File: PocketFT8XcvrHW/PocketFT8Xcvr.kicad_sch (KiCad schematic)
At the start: 55 parts, among them J1 HX8357D SPI, J2 22-23-2021, J3 B5B-XH-A_LF__SN_, J5 HX8357D 8-BIT, Q1 2N7002DW, U1 MCP3422A1T-E/SN, U2 Si4735-D60-GU, U3 SN74ACT244DWR, U4 SI5351C-B-GM, Y1 ASTX-H11-25.000MHZ-T

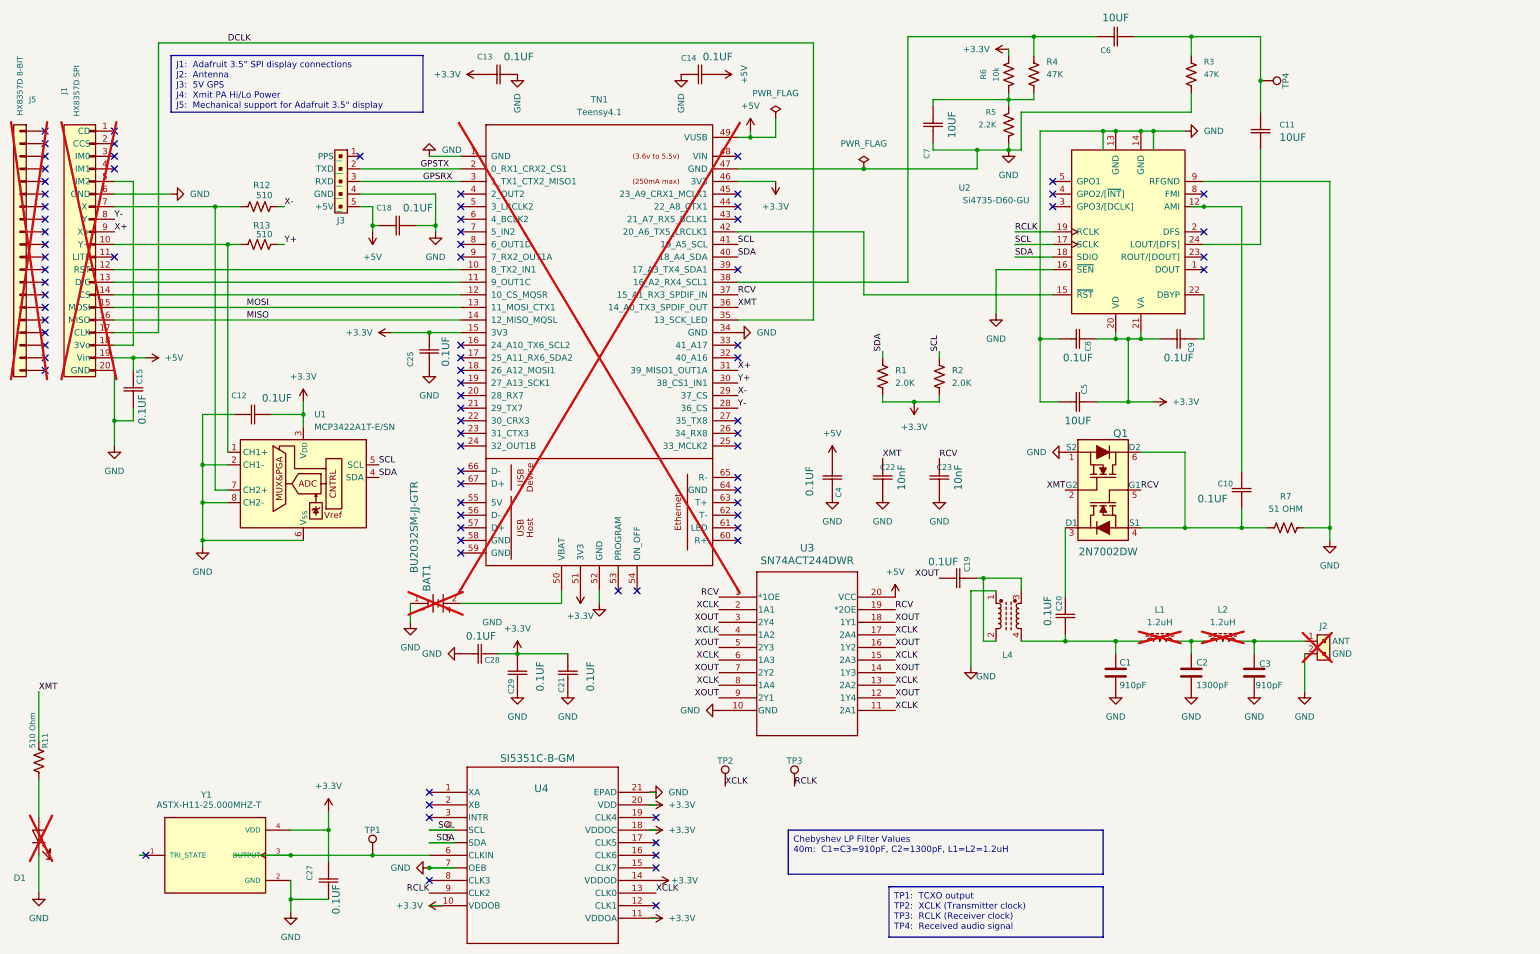
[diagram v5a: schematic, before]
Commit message: Isolate SI4735 I2C traffic from other I2C chips for Issue #23
+ The ADC and SI5351 now reside on SCL2/SDA2.  The SI4735 remains on SCL/SDA.  There are now two I2C bus's.
+ The SI5351 XCLK now drives a single gate re. recommendation for SI5351 phase noise performance.
+ Improved +5V bulk (low frequency) decoupling.
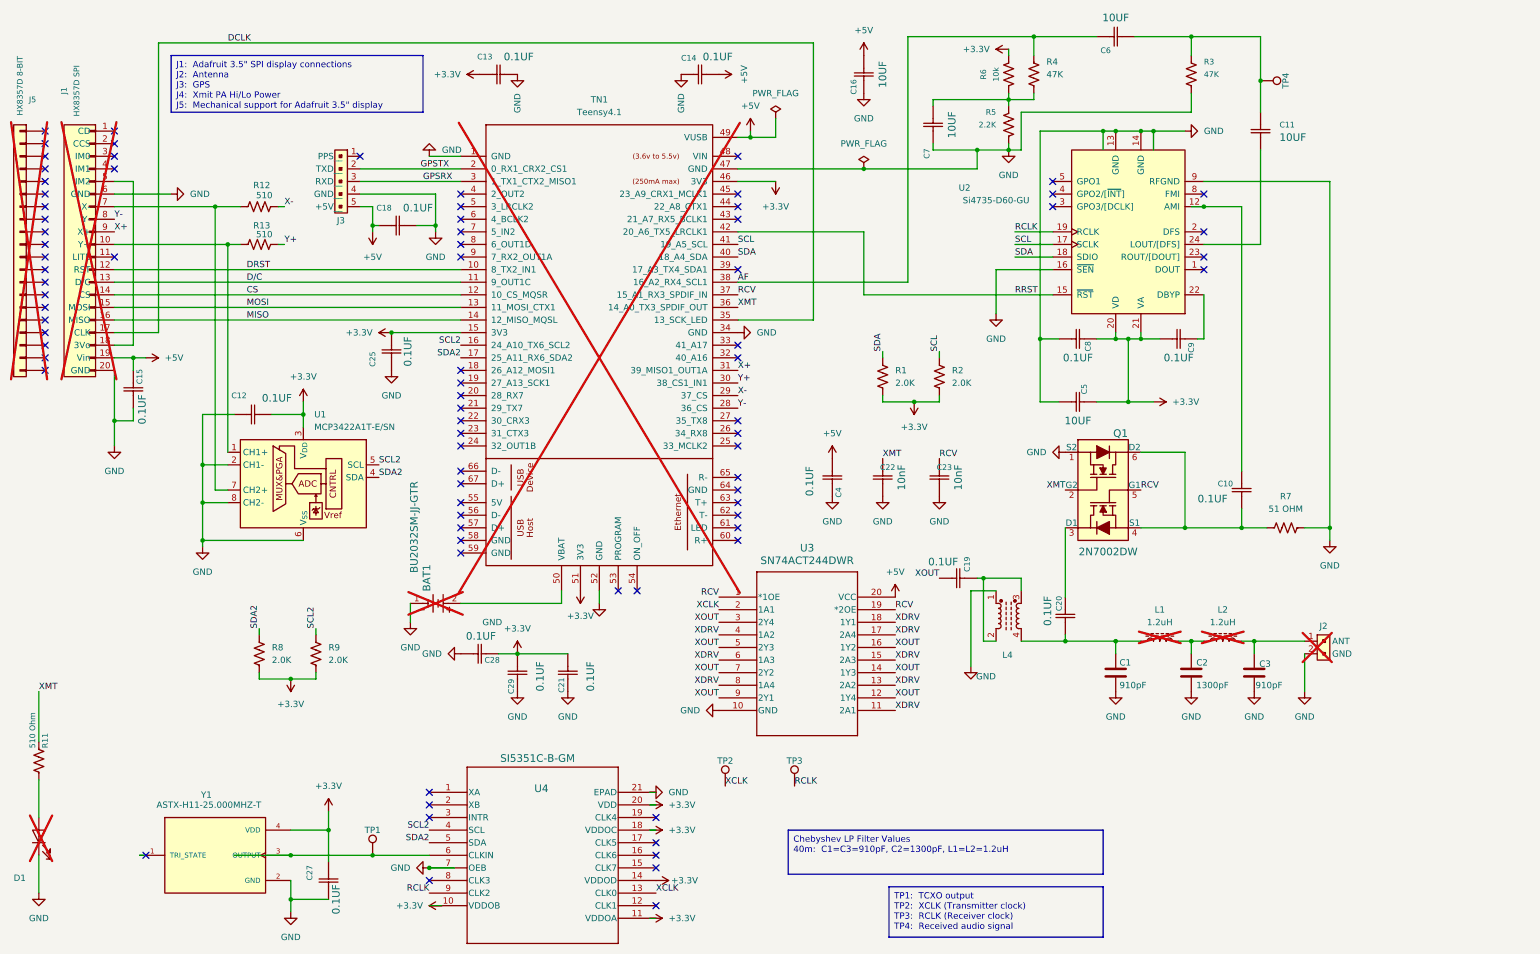
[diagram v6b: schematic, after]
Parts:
- added C16: 10UF, Capacitor_SMD:C_0805_2012Metric, symbol Kemet2024-08-02_22-55-33:C0805C334K4RAC7800
- added R8, R9: 2.0K, Resistor_SMD:R_0603_1608Metric, symbol SparkFun-Resistor:2.0k_0603
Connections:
- net +3.3V: now also R8.2, R9.2
- net +5V: now also C16.2
- net GND: now also C16.1
- net SCL: no longer U1.5 (SCL), U4.4 (SCL)
- net SDA: no longer U1.4 (SDA), U4.5 (SDA)
- net XCLK: no longer U3.11 (2A1), U3.13 (2A2), U3.15 (2A3), U3.17 (2A4), U3.4 (1A2), U3.6 (1A3), U3.8 (1A4)
- net XOUT: no longer U3.18 (1Y1)
- net AF: now reaches C6.2, R4.2, TN1.38 (16_A2_RX4_SCL1)
- net DRST: now reaches J1.12 (RST), TN1.10 (8_TX2_IN1)
- net D/C: now reaches J1.13 (D/C), TN1.11 (9_OUT1C)
- net CS: now reaches J1.14 (CS), TN1.12 (10_CS_MQSR)
- net SCL2: now reaches TN1.16 (24_A10_TX6_SCL2)
- net SCL2: now also U1.5 (SCL), U4.4 (SCL), R9.1
- net SDA2: now reaches TN1.17 (25_A11_RX6_SDA2)
- net SDA2: now also U1.4 (SDA), U4.5 (SDA), R8.1
- net RRST: now reaches TN1.42 (20_A6_TX5_LRCLK1), U2.15 (~{RST})
- new net XDRV: U3.11 (2A1), U3.13 (2A2), U3.15 (2A3), U3.17 (2A4), U3.18 (1Y1), U3.4 (1A2), U3.6 (1A3), U3.8 (1A4)
- no-connect marks 83 -> 81
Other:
- moved on the sheet: C25

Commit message: Ongoing PCB noise mitigations
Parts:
- added C1: 910pF, Capacitor_SMD:C_0805_2012Metric, symbol Device:C
- added L1: 1.2uH, Inductor_THT:L_Toroid_Vertical_L10.0mm_W5.0mm_P5.08mm, symbol Device:L_Ferrite
- renumbered C1 to C2, C2 to C3, C4 to C30, C3 to C4, L1 to L2, L2 to L3
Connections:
- net GND: now also C1.2
- net at C20.2, L4.4: now also C1.1, L1.1; no longer C2.1, L2.1
- net LOUT: now reaches C11.1, U2.24 (LOUT/[DFS])
- net AMI: now reaches C10.2, U2.12 (AMI)
- net XD-: now reaches J1.7 (X-), R12.1, U1.7 (CH2+)
- net YD+: now reaches J1.10 (Y+), R13.1, U1.1 (CH1+)
- net X+ renamed XD+
- net Y- renamed YD-
- new net: C2.1, L1.2, L2.1
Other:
- moved on the sheet: C2, C3, C4, J2, L2, L3

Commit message: Preparing V2.00 board for fab
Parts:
- removed C1, C2, C4: 910pF, Capacitor_SMD:C_0805_2012Metric, symbol Device:C
- removed C3: 1300pF, Capacitor_SMD:C_0805_2012Metric, symbol Device:C
- removed J2: 22-23-2021, digikey-footprints:PinHeader_1x2_P2.54mm_Drill1.02mm, symbol dk_Rectangular-Connectors-Headers-Male-Pins:22-23-2021
- removed L1, L2, L3: 1.2uH, Inductor_THT:L_Toroid_Vertical_L10.0mm_W5.0mm_P5.08mm, symbol Device:L_Ferrite
- added FL1: ~, Filters:PluginFilter, symbol Filters:PluginFilter
- added J2: CONN SMA JACK STR 50OHM EDGE MNT, digikey-footprints:RF_SMA_BoardEdge_142-0701-801, symbol dk_Coaxial-Connectors-RF:142-0701-801
- added TP5, TP6: PTH, SparkFun-Connector:1x01, symbol SparkFun-Connector:TestPoint_PTH
- J3, TP1, TP2, TP3, TP4: now not fitted
- L1: renamed from L4; now not fitted
- Q1: MPN 2N7002DW -> (none); Notes: (none) -> Do not substitute; Type SMT -> SMD
- R12, R13: value 510 -> 510 OHMS; Mfg Part # RC0603JR-072KL -> RC0603JR-07510RL
- R5: value 2.2K -> 2.2K OHM; Mfg Part # (none) -> RES 2.2K OHM 5% 1/10W 0603
- R6: value 10k -> 10k OHM; Mfg Part # (none) -> 10K 5% 1/10W 0603
- U1: Notes (none) -> Do not substitute
- U3: Manufacturer (none) -> TI; Mfg Part # (none) -> SN74ACT244DWR; Notes (none) -> Do not substitute; Type (none) -> SMD
- U4: Type SMT -> SMD
- Y1: Known Supplier (none) -> Mouser Part 815-ASTX-H11-25T; Notes (none) -> Do not substitute
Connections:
- net GND: now also FL1.2 (GND), FL1.4 (GND), J2.2
- net RCV: now also TP6.1
- net XMT: now also TP5.1
- net at C20.2, L1.4: now also FL1.1 (IN)
- new net: FL1.3 (OUT), J2.1
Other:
- title: Idaho Edition of the Pocket FT8 Transceiver -> KQ7B Edition of the Pocket FT8 Transceiver
